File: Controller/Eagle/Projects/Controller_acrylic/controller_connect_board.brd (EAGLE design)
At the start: 185 x 33 mm, 16 parts, among them J1 JST_3PIN_GND_VDD_SIG, J2 JST_3PIN_GND_VDD_SIG, J3 JST_3PIN_GND_VDD_SIG, J4 JST_3PIN_GND_VDD_SIG, J5 GIMBAL_3PIN_MATCH_TDOCU

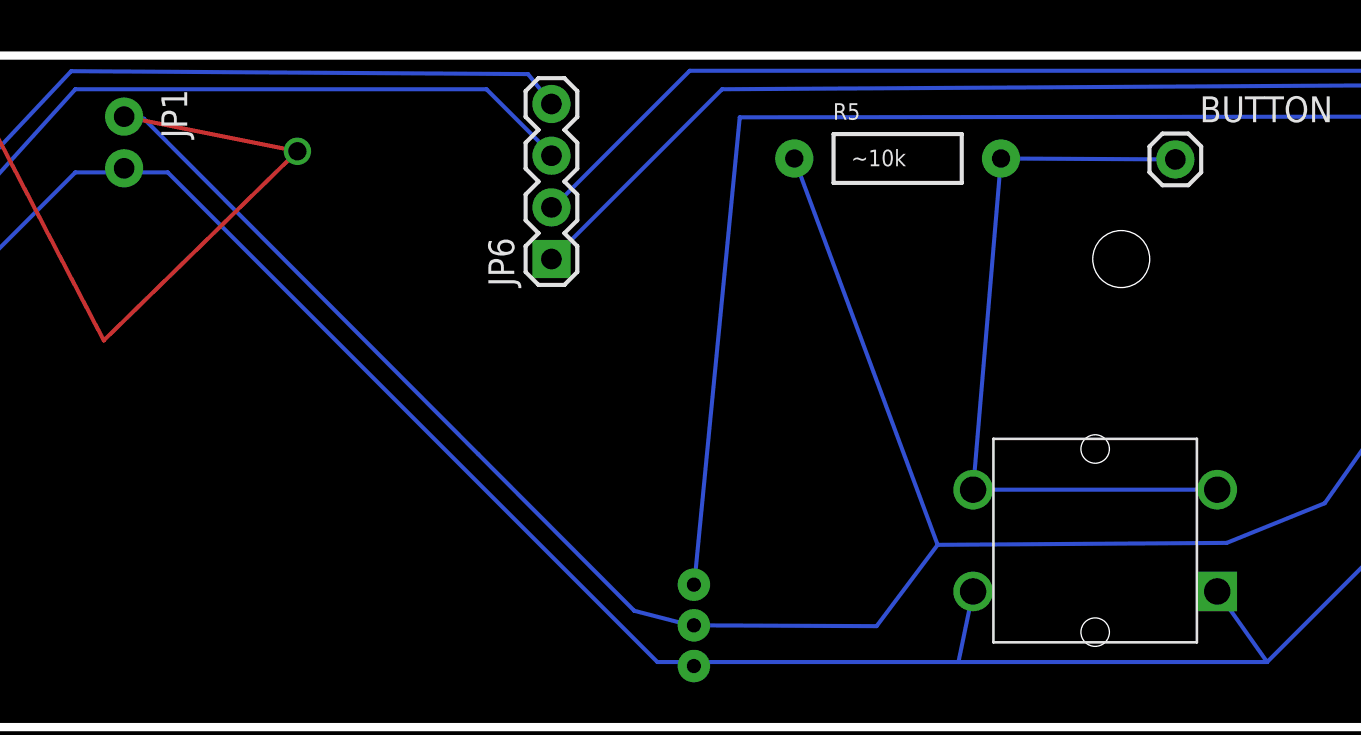
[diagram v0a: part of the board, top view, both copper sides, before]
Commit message: Had to make some holes larger on button for board mill Violated tRestrict
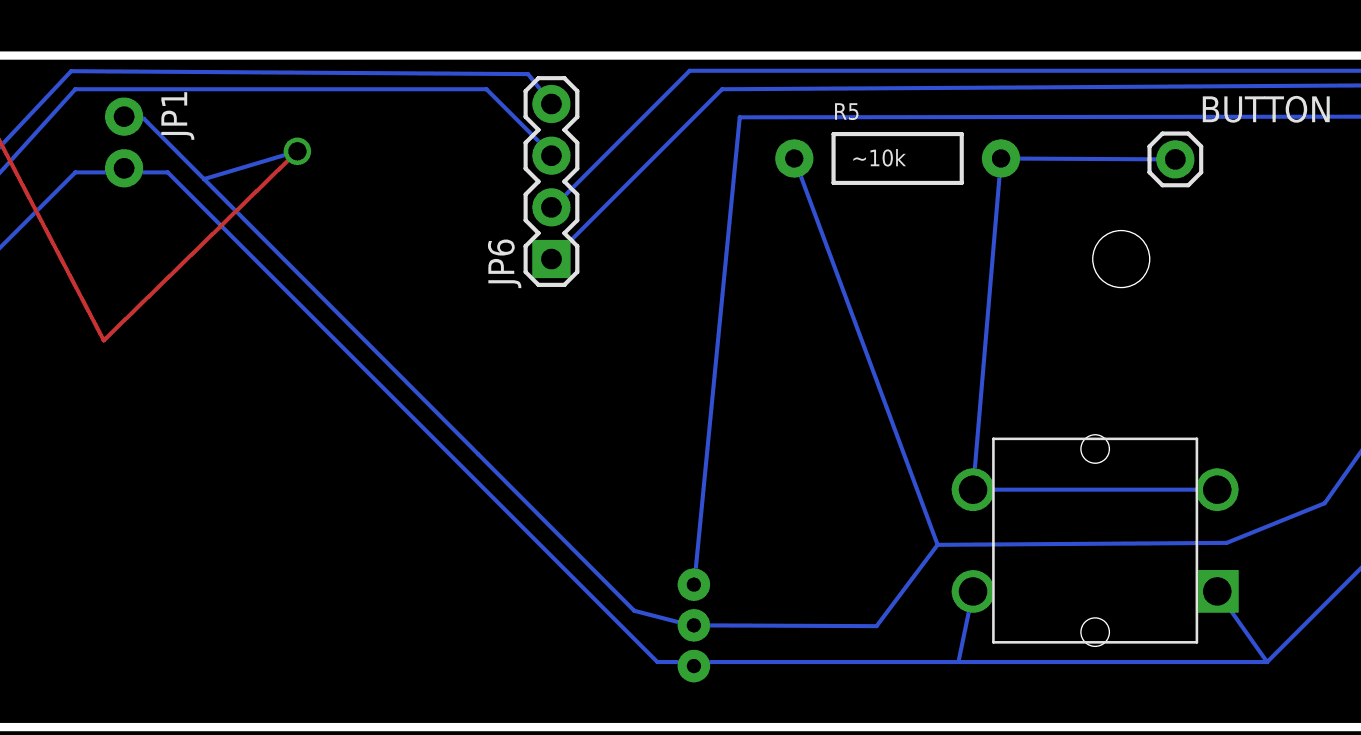
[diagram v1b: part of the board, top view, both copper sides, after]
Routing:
- net GND: track 209.4 -> 205.5 mm
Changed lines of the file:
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@@
 <wire x1="82.855" y1="51.075" x2="83" y2="51" width="0.2" layer="16"/>
 <wire x1="130.071" y1="27.715" x2="132.795" y2="27.013" width="0.2" layer="16"/>
-<wire x1="105.968" y1="51.9" x2="122.40503125" y2="35.40705" width="0.2" layer="16"/>
+<wire x1="105.968" y1="51.9" x2="108.92884375" y2="48.929084375" width="0.2" layer="16"/>
+<wire x1="108.92884375" y1="48.929084375" x2="122.40503125" y2="35.40705" width="0.2" layer="16"/>
 <wire x1="122.40503125" y1="35.40705" x2="130.071" y2="27.715" width="0.2" layer="16"/>
 <wire x1="132.795" y1="27.013" x2="133" y2="27" width="0.2" layer="16"/>
@@
 <via x="97.909" y="52.665" extent="1-16" drill="0.9"/>
 <via x="113.515" y="50.296" extent="1-16" drill="0.9"/>
-<wire x1="105" y1="52" x2="113.515" y2="50.296" width="0.2" layer="1"/>
 <wire x1="97.909" y1="52.665" x2="104" y2="41" width="0.2" layer="1"/>
 <wire x1="104" y1="41" x2="113.515" y2="50.296" width="0.2" layer="1"/>
@@
 <wire x1="141.977" y1="26.96" x2="133" y2="27" width="0.2" layer="16"/>
 <wire x1="144.977" y1="30.956" x2="137.933" y2="49.942" width="0.2" layer="16"/>
+<wire x1="113.515" y1="50.296" x2="108.92884375" y2="48.929084375" width="0.2" layer="16"/>
 </signal>
 <signal name="N$1">

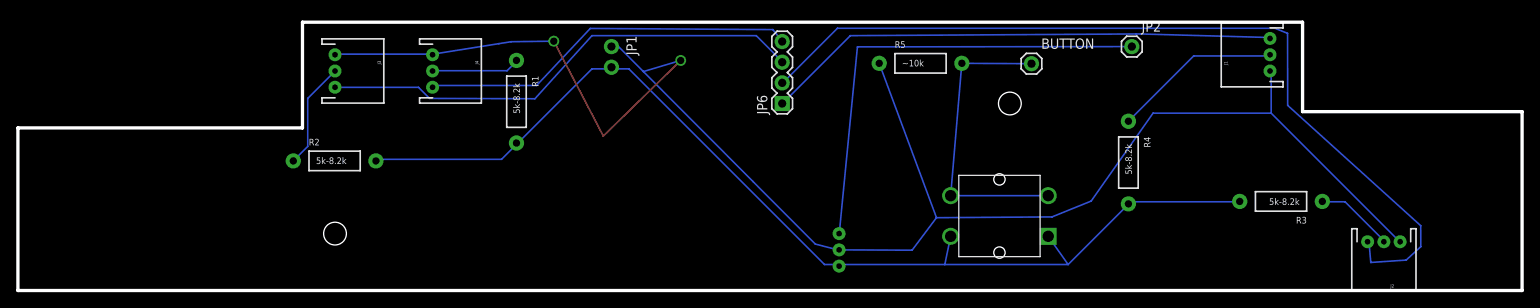
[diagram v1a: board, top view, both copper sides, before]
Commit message: Added dxf files Changed resistor values to 5.6k to be consistent with BOM
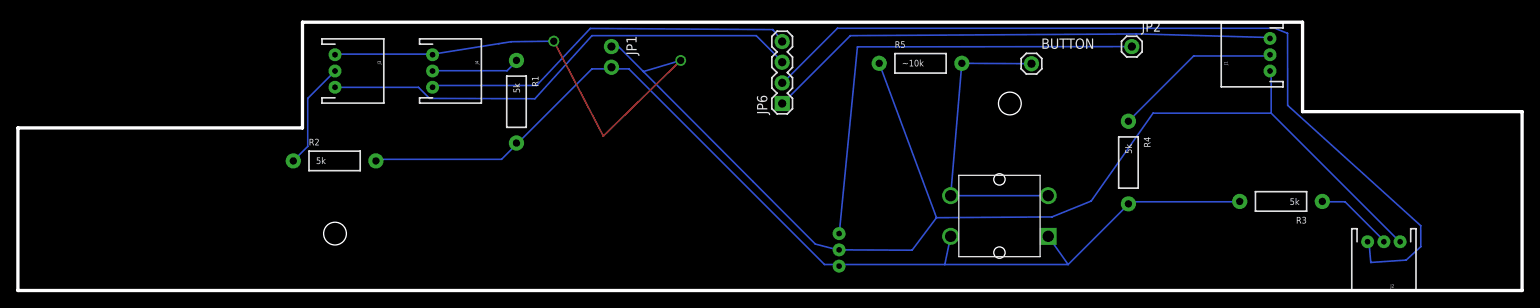
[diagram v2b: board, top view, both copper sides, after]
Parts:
- R1, R2, R3, R4: value 5k-8.2k -> 5k
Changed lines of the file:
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@@
 <element name="J3" library="Controller" package="JST-3-PTH-REVERSE" value="JST_3PIN_GND_VDD_SIG" x="71" y="49" rot="R270"/>
 <element name="J4" library="Controller" package="JST-3-PTH-REVERSE" value="JST_3PIN_GND_VDD_SIG" x="83" y="49" rot="R270"/>
-<element name="R1" library="SparkFun-Resistors" package="AXIAL-0.4" value="5k-8.2k" x="93.318003125" y="45.219046875" rot="R270"/>
-<element name="R2" library="SparkFun-Resistors" package="AXIAL-0.4" value="5k-8.2k" x="70.949403125" y="37.939940625"/>
-<element name="R3" library="SparkFun-Resistors" package="AXIAL-0.4" value="5k-8.2k" x="187.352325" y="32.957490625" rot="R180"/>
-<element name="R4" library="SparkFun-Resistors" package="AXIAL-0.4" value="5k-8.2k" x="168.58266875" y="37.739028125" rot="R270"/>
+<element name="R1" library="SparkFun-Resistors" package="AXIAL-0.4" value="5k" x="93.318003125" y="45.219046875" rot="R270"/>
+<element name="R2" library="SparkFun-Resistors" package="AXIAL-0.4" value="5k" x="70.949403125" y="37.939940625"/>
+<element name="R3" library="SparkFun-Resistors" package="AXIAL-0.4" value="5k" x="187.352325" y="32.957490625" rot="R180"/>
+<element name="R4" library="SparkFun-Resistors" package="AXIAL-0.4" value="5k" x="168.58266875" y="37.739028125" rot="R270"/>
 <element name="JP6" library="SparkFun-Connectors" package="1X04" value="" x="126" y="45" rot="R90"/>
 <element name="JP1" library="SparkFun-Connectors" package="1X02_NO_SILK" value="" x="105" y="52" rot="R270"/>
